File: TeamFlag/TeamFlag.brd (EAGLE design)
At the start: 40.6 x 40.6 mm, 24 parts, among them IC1 ARDUINO_PRO_MICROSMD, Q3 N-CH, Q4 N-CH

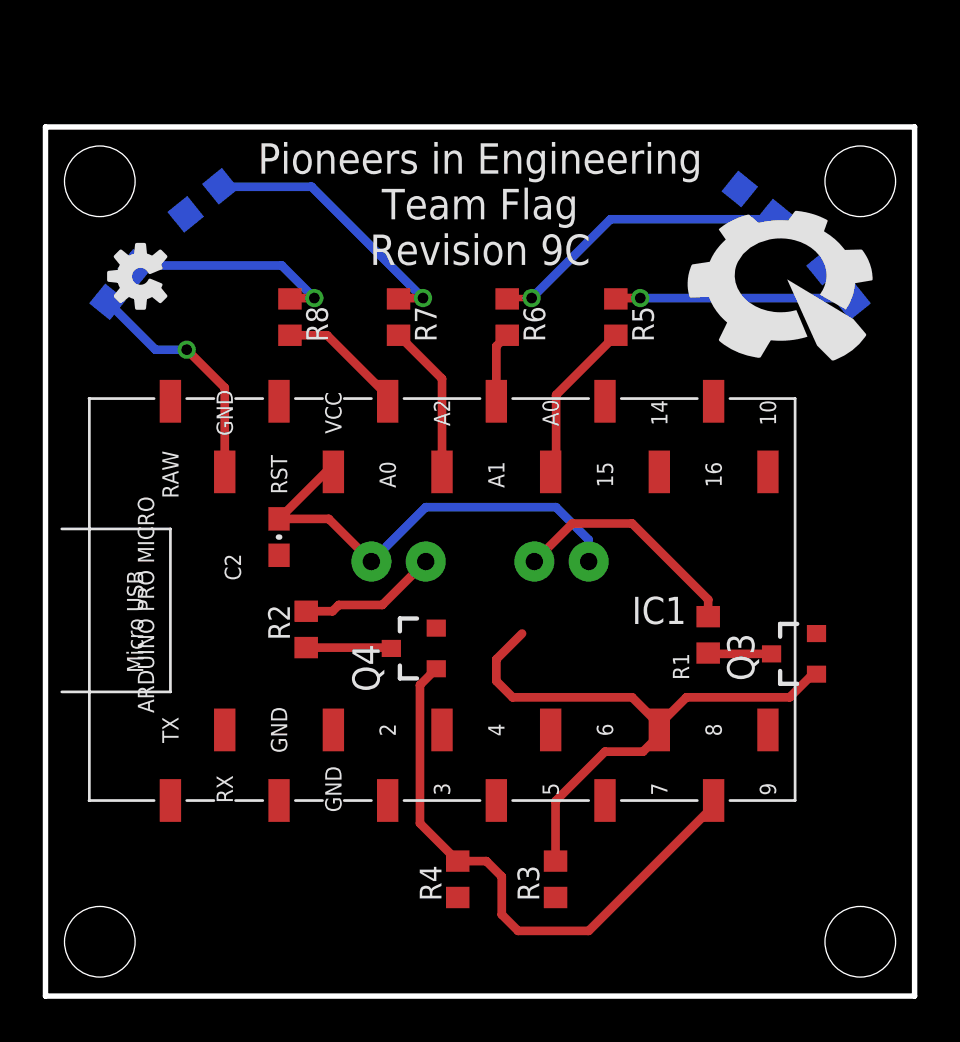
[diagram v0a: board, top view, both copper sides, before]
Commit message: Update LEDs on teamflag
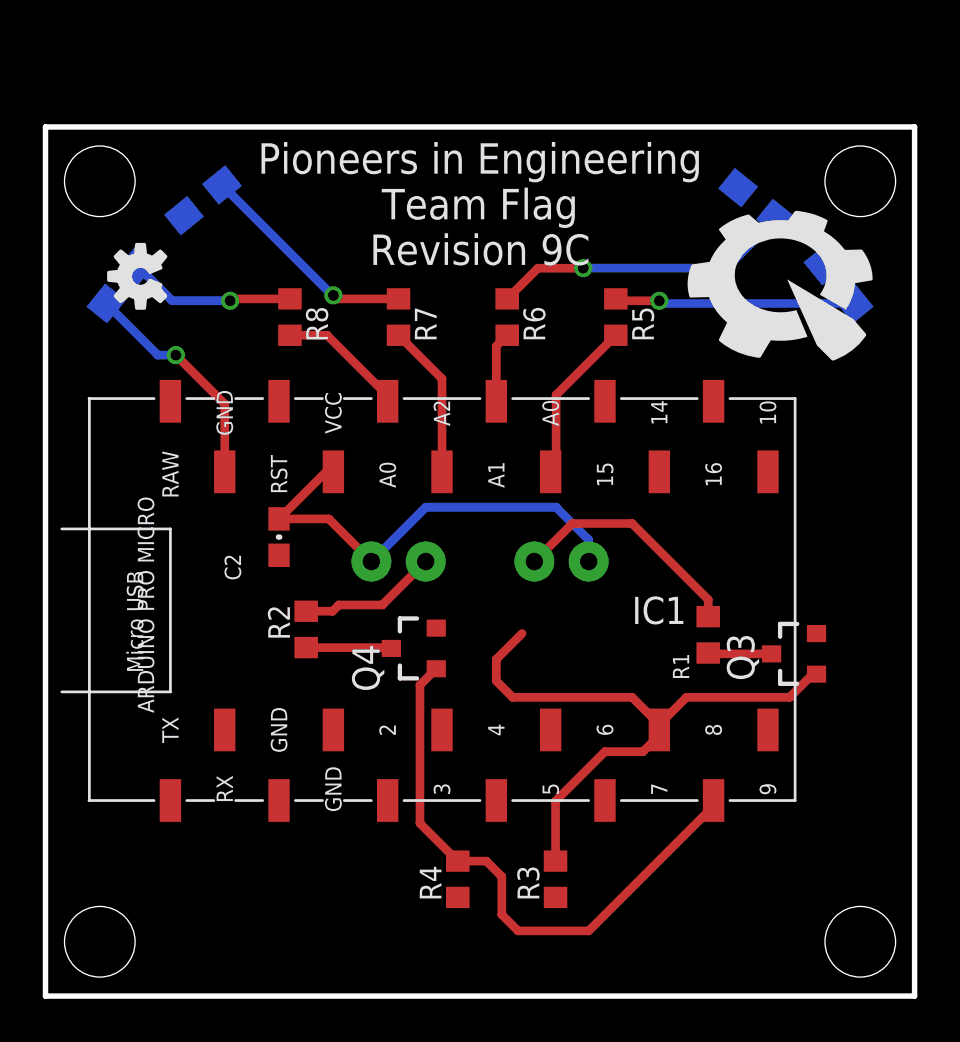
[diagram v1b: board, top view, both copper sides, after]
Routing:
- net LED3R: track 12.8 -> 10.5 mm
- net LED4R: track 10.2 -> 7.87 mm
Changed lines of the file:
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@@
 <contactref element="IC1" pad="2"/>
 <contactref element="IC1" pad="3"/>
-<wire x1="8.382" y1="24.513" x2="8.382" y2="28.448" width="0.4064" layer="1"/>
-<wire x1="8.382" y1="28.448" x2="6.604" y2="30.226" width="0.4064" layer="1"/>
-<via x="6.604" y="30.226" extent="1-16" drill="0.5"/>
-<wire x1="6.604" y1="30.226" x2="5.13930625" y2="30.226" width="0.4064" layer="16"/>
-<wire x1="5.13930625" y1="30.226" x2="2.900628125" y2="32.464678125" width="0.4064" layer="16"/>
 <contactref element="Q3" pad="2"/>
 <contactref element="R3" pad="1"/>
 <contactref element="Q4" pad="2"/>
 <contactref element="R4" pad="1"/>
+<wire x1="2.8366875" y1="32.385721875" x2="5.250409375" y2="29.972" width="0.4064" layer="16"/>
+<wire x1="5.250409375" y1="29.972" x2="6.096" y2="29.972" width="0.4064" layer="16"/>
+<via x="6.096" y="29.972" extent="1-16" drill="0.5"/>
+<wire x1="6.096" y1="29.972" x2="8.382" y2="27.686" width="0.4064" layer="1"/>
+<wire x1="8.382" y1="27.686" x2="8.382" y2="24.513" width="0.4064" layer="1"/>
 </signal>
 <signal name="BLUE(IO1)">
@@
 <contactref element="R5" pad="1"/>
 <contactref element="LED1" pad="A"/>
-<via x="27.813" y="32.639" extent="1-16" drill="0.5"/>
-<wire x1="37.565053125" y1="32.639" x2="37.739375" y2="32.464678125" width="0.3048" layer="16"/>
-<wire x1="26.67" y1="32.6" x2="26.709" y2="32.639" width="0.3048" layer="1"/>
-<wire x1="26.709" y1="32.639" x2="27.813" y2="32.639" width="0.4064" layer="1"/>
-<wire x1="37.565053125" y1="32.639" x2="27.813" y2="32.639" width="0.4064" layer="16"/>
+<wire x1="37.803315625" y1="32.385721875" x2="28.828278125" y2="32.385721875" width="0.4064" layer="16"/>
+<wire x1="28.828278125" y1="32.385721875" x2="28.702" y2="32.512" width="0.4064" layer="16"/>
+<via x="28.702" y="32.512" extent="1-16" drill="0.5"/>
+<wire x1="28.702" y1="32.512" x2="26.758" y2="32.512" width="0.4064" layer="1"/>
+<wire x1="26.758" y1="32.512" x2="26.67" y2="32.6" width="0.4064" layer="1"/>
 </signal>
 <signal name="LED2R">
 <contactref element="R6" pad="1"/>
 <contactref element="LED2" pad="A"/>
-<wire x1="34.083321875" y1="36.428625" x2="33.976696875" y2="36.322" width="0.3048" layer="16"/>
-<via x="22.733" y="32.639" extent="1-16" drill="0.5"/>
-<wire x1="21.59" y1="32.6" x2="21.629" y2="32.639" width="0.3048" layer="1"/>
-<wire x1="21.629" y1="32.639" x2="22.733" y2="32.639" width="0.3048" layer="1"/>
-<wire x1="33.976696875" y1="36.322" x2="26.416" y2="36.322" width="0.4064" layer="16"/>
-<wire x1="26.416" y1="36.322" x2="22.733" y2="32.639" width="0.4064" layer="16"/>
+<wire x1="34.162278125" y1="36.364684375" x2="31.83359375" y2="34.036" width="0.4064" layer="16"/>
+<wire x1="31.83359375" y1="34.036" x2="25.146" y2="34.036" width="0.4064" layer="16"/>
+<via x="25.146" y="34.036" extent="1-16" drill="0.5"/>
+<wire x1="25.146" y1="34.036" x2="23.026" y2="34.036" width="0.4064" layer="1"/>
+<wire x1="23.026" y1="34.036" x2="21.59" y2="32.6" width="0.4064" layer="1"/>
 </signal>
 <signal name="LED3R">
 <contactref element="R7" pad="1"/>
 <contactref element="LED3" pad="A"/>
-<via x="17.653" y="32.639" extent="1-16" drill="0.5"/>
-<wire x1="8.19569375" y1="37.846" x2="8.175321875" y2="37.866371875" width="0.3048" layer="16"/>
-<wire x1="16.51" y1="32.6" x2="16.549" y2="32.639" width="0.3048" layer="1"/>
-<wire x1="16.549" y1="32.639" x2="17.653" y2="32.639" width="0.4064" layer="1"/>
-<wire x1="8.19569375" y1="37.846" x2="12.446" y2="37.846" width="0.4064" layer="16"/>
-<wire x1="12.446" y1="37.846" x2="17.653" y2="32.639" width="0.4064" layer="16"/>
+<wire x1="8.254278125" y1="37.9303125" x2="13.418590625" y2="32.766" width="0.4064" layer="16"/>
+<wire x1="13.418590625" y1="32.766" x2="13.462" y2="32.766" width="0.4064" layer="16"/>
+<via x="13.462" y="32.766" extent="1-16" drill="0.5"/>
+<wire x1="13.462" y1="32.766" x2="13.628" y2="32.6" width="0.4064" layer="1"/>
+<wire x1="13.628" y1="32.6" x2="16.51" y2="32.6" width="0.4064" layer="1"/>
 </signal>
 <signal name="LED4R">
 <contactref element="R8" pad="1"/>
 <contactref element="LED4" pad="A"/>
-<via x="12.573" y="32.639" extent="1-16" drill="0.5"/>
-<wire x1="4.29105625" y1="34.163" x2="4.211375" y2="34.08331875" width="0.3048" layer="16"/>
-<wire x1="11.43" y1="32.6" x2="11.469" y2="32.639" width="0.3048" layer="1"/>
-<wire x1="11.469" y1="32.639" x2="12.573" y2="32.639" width="0.4064" layer="1"/>
-<wire x1="4.29105625" y1="34.163" x2="11.049" y2="34.163" width="0.4064" layer="16"/>
-<wire x1="11.049" y1="34.163" x2="12.573" y2="32.639" width="0.4064" layer="16"/>
+<wire x1="4.275315625" y1="34.162275" x2="5.925590625" y2="32.512" width="0.4064" layer="16"/>
+<wire x1="5.925590625" y1="32.512" x2="8.636" y2="32.512" width="0.4064" layer="16"/>
+<via x="8.636" y="32.512" extent="1-16" drill="0.5"/>
+<wire x1="8.636" y1="32.512" x2="8.724" y2="32.6" width="0.4064" layer="1"/>
+<wire x1="8.724" y1="32.6" x2="11.43" y2="32.6" width="0.4064" layer="1"/>
 </signal>
 <signal name="LED1">

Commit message: Remove unnecessary route
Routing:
- net BLUE(IO1): track 28.9 -> 17.6 mm
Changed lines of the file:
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@@
 <wire x1="23.8506" y1="9.1186" x2="26.162" y2="11.43" width="0.4064" layer="1"/>
 <wire x1="26.162" y1="11.43" x2="27.94" y2="11.43" width="0.4064" layer="1"/>
-<wire x1="27.432" y1="13.97" x2="21.844" y2="13.97" width="0.4064" layer="1"/>
-<wire x1="21.844" y1="13.97" x2="21.082" y2="14.732" width="0.4064" layer="1"/>
-<wire x1="21.082" y1="14.732" x2="21.082" y2="15.748" width="0.4064" layer="1"/>
-<wire x1="21.082" y1="15.748" x2="22.286" y2="16.952" width="0.4064" layer="1"/>
 <contactref element="IC1" pad="7"/>
-<wire x1="28.702" y1="12.446" x2="28.702" y2="12.7" width="0.4064" layer="1"/>
-<wire x1="28.702" y1="12.7" x2="27.432" y2="13.97" width="0.4064" layer="1"/>
 <wire x1="28.702" y1="12.446" x2="28.702" y2="12.192" width="0.4064" layer="1"/>
 <wire x1="28.702" y1="12.192" x2="27.94" y2="11.43" width="0.4064" layer="1"/>
 <contactref element="Q3" pad="1"/>
-<wire x1="28.702" y1="12.7" x2="29.972" y2="13.97" width="0.4064" layer="1"/>
-<wire x1="29.972" y1="13.97" x2="34.798" y2="13.97" width="0.4064" layer="1"/>
-<wire x1="34.798" y1="13.97" x2="35.88" y2="15.052" width="0.4064" layer="1"/>
-<wire x1="35.88" y1="15.052" x2="36.052" y2="15.052" width="0.4064" layer="1"/>
+<wire x1="28.702" y1="12.446" x2="30.988" y2="12.446" width="0.4064" layer="1"/>
+<wire x1="30.988" y1="12.446" x2="32.512" y2="13.97" width="0.4064" layer="1"/>
+<wire x1="32.512" y1="13.97" x2="34.97" y2="13.97" width="0.4064" layer="1"/>
+<wire x1="34.97" y1="13.97" x2="36.052" y2="15.052" width="0.4064" layer="1"/>
 </signal>
 <signal name="BSOURCE">

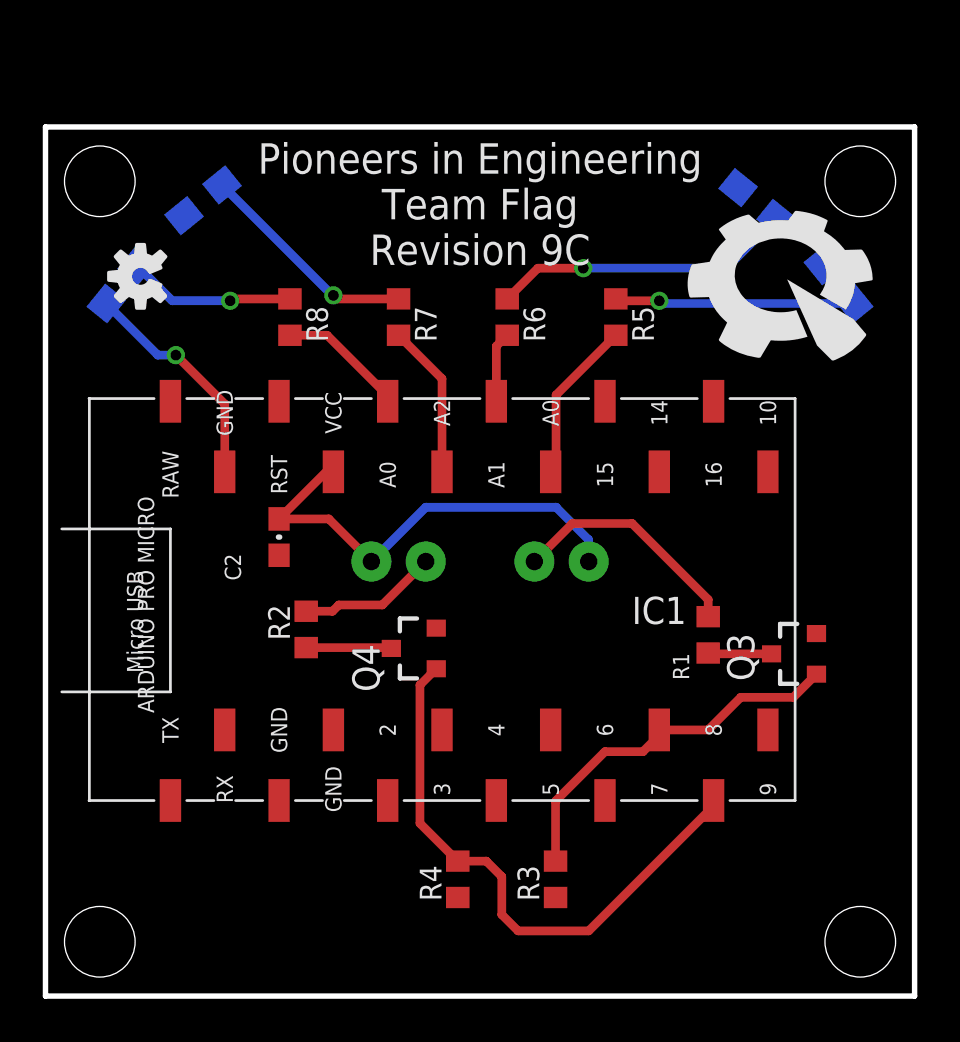
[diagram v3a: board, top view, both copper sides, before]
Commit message: Dimension fixes; tkeepout changes
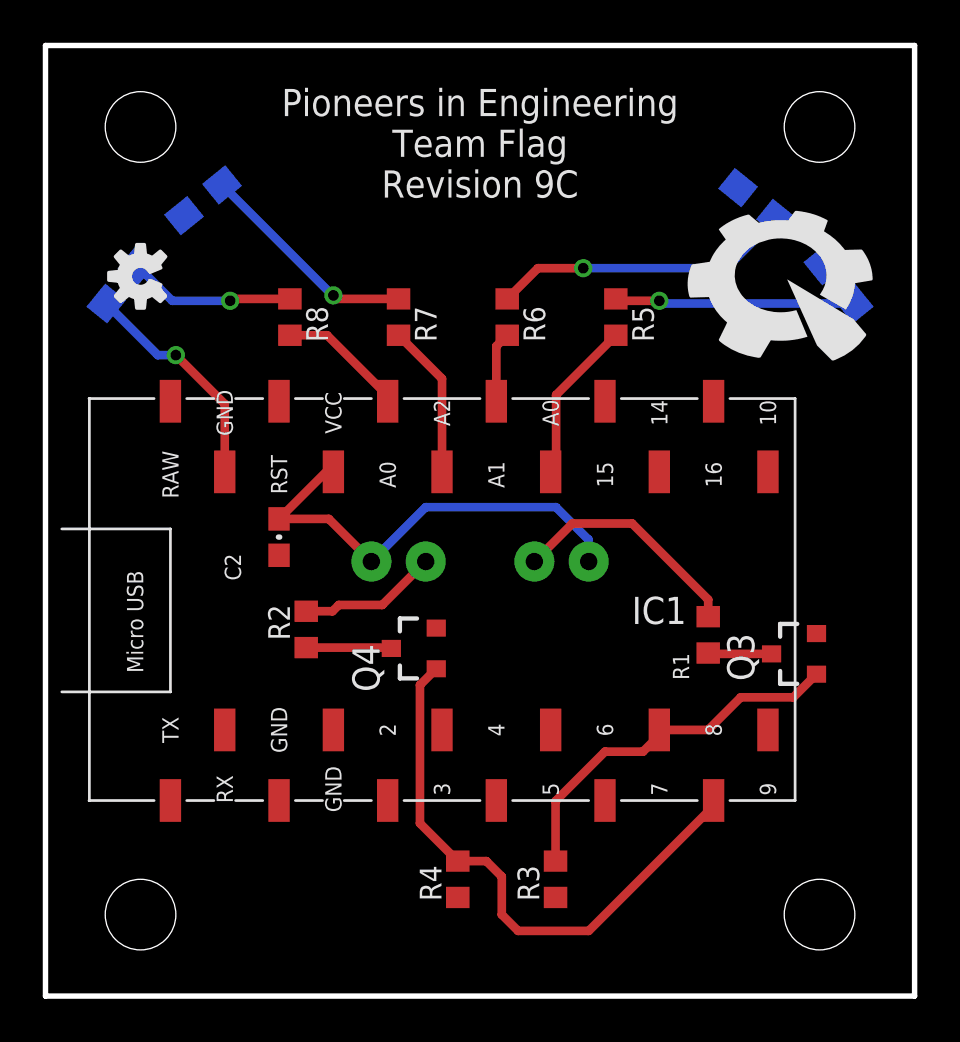
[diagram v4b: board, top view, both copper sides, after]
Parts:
- moved U$11 3.18 mm to (36.2, 40.6)
- moved U$12 3.17 mm to (4.45, 40.6)
- moved U$14 2.29 mm to (36.2, 3.81)
- moved U$13 2.29 mm to (4.45, 3.81)
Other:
- board size 40.6 x 40.6 mm -> 40.6 x 44.5 mm
- board text removed: "ARDUINO PRO MICRO"
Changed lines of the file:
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@@
 <setting verticaltext="up"/>
 </settings>
-<grid distance="0.01" unitdist="inch" unit="inch" style="lines" multiple="1" display="yes" altdistance="0.005" altunitdist="inch" altunit="inch"/>
+<grid distance="0.05" unitdist="inch" unit="inch" style="lines" multiple="1" display="yes" altdistance="0.005" altunitdist="inch" altunit="inch"/>
 <layers>
 <layer number="1" name="Top" color="4" fill="1" visible="yes" active="yes"/>
@@
 <plain>
 <wire x1="40.64" y1="0" x2="0" y2="0" width="0.254" layer="20"/>
-<wire x1="0" y1="0" x2="0" y2="40.64" width="0.254" layer="20"/>
-<wire x1="0" y1="40.64" x2="40.64" y2="40.64" width="0.254" layer="20"/>
-<wire x1="40.64" y1="40.64" x2="40.64" y2="0" width="0.254" layer="20"/>
+<wire x1="0" y1="0" x2="0" y2="44.45" width="0.254" layer="20"/>
+<wire x1="0" y1="44.45" x2="40.64" y2="44.45" width="0.254" layer="20"/>
+<wire x1="40.64" y1="44.45" x2="40.64" y2="0" width="0.254" layer="20"/>
 <circle x="20.32" y="20.32" radius="19.685" width="0.4064" layer="22"/>
 <text x="6.858" y="23.114" size="1.27" layer="22" font="vector" rot="MR180">Yellow</text>
 <text x="27.94" y="23.114" size="1.27" layer="22" font="vector" rot="MR180">Blue</text>
-<text x="20.32" y="39.878" size="1.4224" layer="21" font="vector" ratio="15" rot="R180" align="bottom-center">Pioneers in Engineering
+<text x="20.32" y="42.418" size="1.27" layer="21" font="vector" ratio="15" rot="R180" align="bottom-center">Pioneers in Engineering
 Team Flag
 Revision 9C</text>
@@
 For more information, visit:
 https://github.com/pioneers/SmartSensors</text>
-<text x="4.318" y="23.368" size="0.762" layer="25" font="vector" rot="R270">ARDUINO PRO MICRO</text>
 </plain>
 <attributes>
@@
 <attribute name="VALUE" x="10.033" y="19.431" size="0.762" layer="27" font="vector" ratio="15" rot="R270" align="top-right"/>
 </element>
-<element name="U$11" library="pie" package="STAND-OFF" value="" x="38.1" y="38.1"/>
-<element name="U$12" library="pie" package="STAND-OFF" value="" x="2.54" y="38.1"/>
-<element name="U$13" library="pie" package="STAND-OFF" value="" x="2.54" y="2.54"/>
-<element name="U$14" library="pie" package="STAND-OFF" value="" x="38.1" y="2.54"/>
+<element name="U$11" library="pie" package="STAND-OFF" value="" x="36.195" y="40.64"/>
+<element name="U$12" library="pie" package="STAND-OFF" value="" x="4.445" y="40.64"/>
+<element name="U$13" library="pie" package="STAND-OFF" value="" x="4.445" y="3.81"/>
+<element name="U$14" library="pie" package="STAND-OFF" value="" x="36.195" y="3.81"/>
 <element name="R5" library="pie" package="R0603" value="130" x="26.67" y="31.75" smashed="yes" rot="R270">
 <attribute name="MANUFACTURER" value="Rohm Semiconductor" x="26.67" y="31.75" size="1.778" layer="27" rot="R270" display="off"/>
@@
 <contactref element="C2" pad="2"/>
 <polygon width="0.4064" layer="1">
-<vertex x="0" y="40.64"/>
-<vertex x="40.64" y="40.64"/>
+<vertex x="0" y="44.45"/>
+<vertex x="40.64" y="44.45"/>
 <vertex x="40.64" y="0"/>
 <vertex x="0" y="0"/>
@@
 <vertex x="40.64" y="0"/>
 <vertex x="0" y="0"/>
-<vertex x="0" y="40.64"/>
-<vertex x="40.64" y="40.64"/>
+<vertex x="0" y="44.45"/>
+<vertex x="40.64" y="44.45"/>
 </polygon>
 <contactref element="IC1" pad="GND@3"/>
